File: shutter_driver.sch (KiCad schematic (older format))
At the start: 41 parts, among them J1 SHUTTER, J2 POWER, J3 I/O, J4 FRONT, Q1 2N3904, Q2 FQP30N06L-ND, Q3 2N3904, Q4 2N3904, Q5 Q_PMOS_GDS, SW1 SW_DPDT_x2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

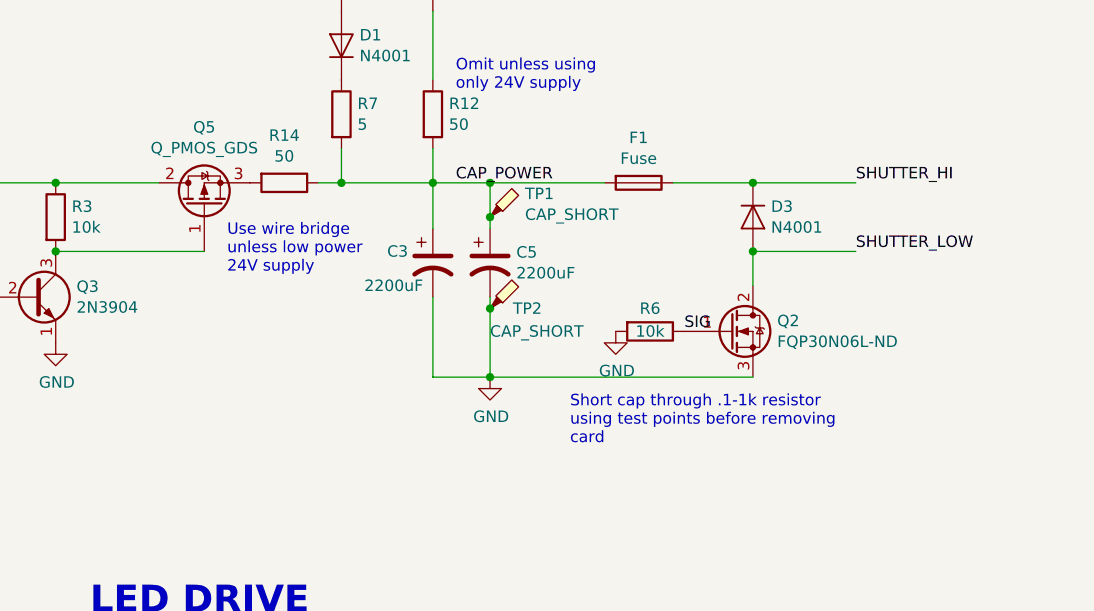
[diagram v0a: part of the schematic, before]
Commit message: fixed backward pmos
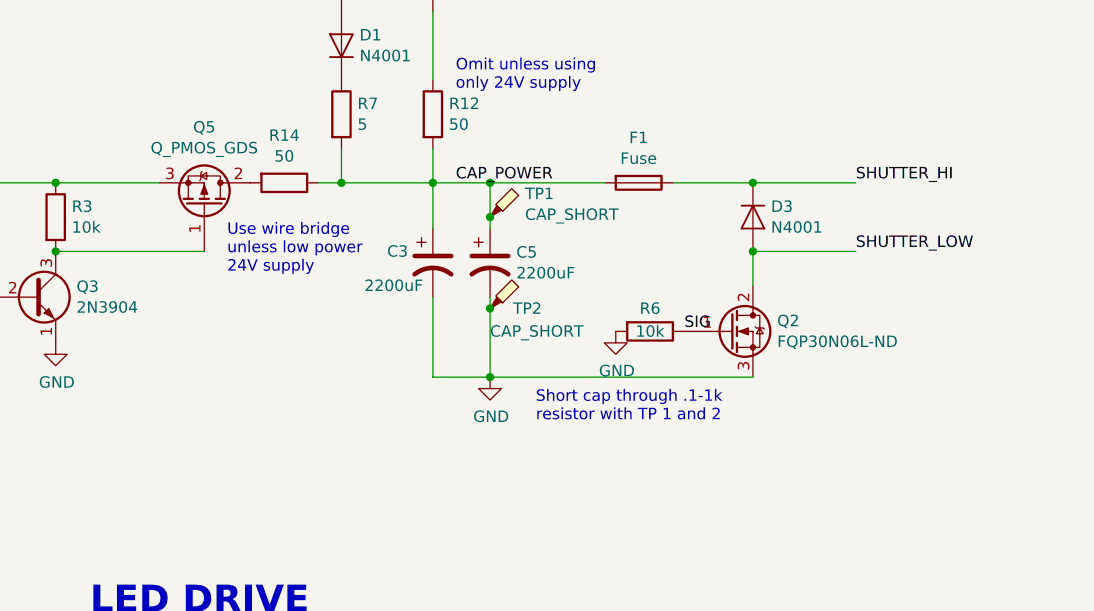
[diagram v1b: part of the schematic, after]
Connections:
- net +24V: now also Q5.3 (S); no longer Q5.2 (D)
- net at R14.2: now also Q5.2 (D); no longer Q5.3 (S)
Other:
- note added: "Short cap through .1-1k \nresistor with TP 1 and 2"
- note removed: "Short cap through .1-1k resistor\nusing test points before removing\ncard"
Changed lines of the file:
@@
 Sheet 1 1
 Title "NM LST400 Shutter Driver"
-Date ""
+Date "5.21.19"
 Rev "2.0"
 Comp "CSU Ultra Cold"
@@
 Wire Wire Line
 	4300 2500 4300 2800
-Text Notes 4650 3100 0    50   ~ 0
-Short cap through .1-1k resistor\nusing test points before removing\ncard
+Text Notes 4500 3000 0    50   ~ 0
+Short cap through .1-1k \nresistor with TP 1 and 2
 Wire Wire Line
 	4300 2800 5450 2800
@@
 F 3 "~" H 3050 2050 50  0001 C CNN
 	1    3050 2050
-	0    -1   -1   0
-$EndComp
-Wire Wire Line
+	0    1    -1   0
+$EndComp
+Wire Wire Line

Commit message: minor fixes including filter caps on rails of gates and comparator. note PMOS flipped in last commit.
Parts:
- added C2, C4, C7: .1u, symbol Device:C
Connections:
- net +5V: now also C2.2, C4.2, C7.2
- net GND: now also C2.1, C4.1, C7.1
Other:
- note added: "Pot sets interupt trigger point. \n2.5v is good starting point"
- note removed: "Pot sets interupt trigger point. \n2.5 v is good starting point"
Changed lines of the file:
@@
 Title "NM LST400 Shutter Driver"
 Date "5.21.19"
-Rev "2.0"
+Rev "2.1"
 Comp "CSU Ultra Cold"
 Comment1 ""
@@
 U 1 1 5C953346
 P 7600 4950
-F 0 "U6" H 7600 5275 50  0000 C CNN
-F 1 "SN74LVC1G86" H 7600 5184 50  0000 C CNN
+F 0 "U6" H 7550 4950 50  0000 C CNN
+F 1 "SN74LVC1G86" H 7300 5150 50  0000 C CNN
 F 2 "TO_SOT_Packages_SMD:SOT-23-5_HandSoldering" H 7600 4950 50  0001 C CNN
 F 3 "http://www.ti.com/lit/ds/symlink/sn74lvc1g86.pdf" H 7600 4950 50  0001 C CNN
@@
 U 1 1 5C97A9A3
 P 10250 2900
-F 0 "U9" V 10204 3088 50  0000 L CNN
-F 1 "SN74LVC1G86" V 10295 3088 50  0000 L CNN
+F 0 "U9" V 10200 2850 50  0000 L CNN
+F 1 "SN74LVC1G86" V 10050 3000 50  0000 L CNN
 F 2 "TO_SOT_Packages_SMD:SOT-23-5_HandSoldering" H 10250 2900 50  0001 C CNN
 F 3 "http://www.ti.com/lit/gpn/sn74HC86" H 10250 2900 50  0001 C CNN
@@
 SIG
 Text Notes 9050 5950 0    50   ~ 0
-Pot sets interupt trigger point. \n2.5 v is good starting point
+Pot sets interupt trigger point. \n2.5v is good starting point
 $Comp
 L Connector:TestPoint_Probe TP4
@@
 Text Label 2250 5150 1    50   ~ 0
 SHUTTER_RET
-Text Notes 9600 4450 0    50   ~ 0
+Text Notes 7450 5450 0    50   ~ 0
 RC network sets interupt time
 $Comp
@@
 Text Label 9900 1800 3    50   ~ 0
 LED_G-
-Text Notes 9850 1100 0    50   ~ 0
-RC network sets interupt time
 $Comp
 L Connector:Screw_Terminal_01x06 J4
@@
 L power:+5V #PWR0112
 U 1 1 5CB4EB9D
-P 7600 4850
-F 0 "#PWR0112" H 7600 4700 50  0001 C CNN
-F 1 "+5V" H 7615 5023 50  0000 C CNN
-F 2 "" H 7600 4850 50  0001 C CNN
-F 3 "" H 7600 4850 50  0001 C CNN
-	1    7600 4850
+P 7600 4650
+F 0 "#PWR0112" H 7600 4500 50  0001 C CNN
+F 1 "+5V" H 7500 4700 50  0000 C CNN
+F 2 "" H 7600 4650 50  0001 C CNN
+F 3 "" H 7600 4650 50  0001 C CNN
+	1    7600 4650
 	1    0    0    -1
 $EndComp
@@
 L power:+5V #PWR0113
 U 1 1 5CB4FC33
-P 10350 2900
-F 0 "#PWR0113" H 10350 2750 50  0001 C CNN
-F 1 "+5V" V 10365 3028 50  0000 L CNN
-F 2 "" H 10350 2900 50  0001 C CNN
-F 3 "" H 10350 2900 50  0001 C CNN
-	1    10350 2900
+P 10400 2900
+F 0 "#PWR0113" H 10400 2750 50  0001 C CNN
+F 1 "+5V" V 10415 3028 50  0000 L CNN
+F 2 "" H 10400 2900 50  0001 C CNN
+F 3 "" H 10400 2900 50  0001 C CNN
+	1    10400 2900
 	0    1    1    0
 $EndComp
@@
 Wire Wire Line
 	10250 3150 10250 3200
+$Comp
+L Device:C C2
+U 1 1 5CE5325D
+P 7750 4650
+F 0 "C2" V 7498 4650 50  0000 C CNN
+F 1 ".1u" V 7589 4650 50  0000 C CNN
+F 2 "" H 7788 4500 50  0001 C CNN
+F 3 "~" H 7750 4650 50  0001 C CNN
+	1    7750 4650
+	0    1    1    0
+$EndComp
+Connection ~ 7600 4650
+$Comp
+L power:GND #PWR0114
+U 1 1 5CE5337A
+P 7900 4650
+F 0 "#PWR0114" H 7900 4400 50  0001 C CNN
+F 1 "GND" V 7905 4522 50  0000 R CNN
+F 2 "" H 7900 4650 50  0001 C CNN
+F 3 "" H 7900 4650 50  0001 C CNN
+	1    7900 4650
+	0    -1   -1   0
+$EndComp
+$Comp
+L Device:C C7
+U 1 1 5CE535B0
+P 10400 3050
+F 0 "C7" V 10550 3050 50  0000 C CNN
+F 1 ".1u" V 10450 3150 50  0000 C CNN
+F 2 "" H 10438 2900 50  0001 C CNN
+F 3 "~" H 10400 3050 50  0001 C CNN
+	1    10400 3050
+	1    0    0    1
+$EndComp
+$Comp
+L power:GND #PWR0115
+U 1 1 5CE535B7
+P 10400 3200
+F 0 "#PWR0115" H 10400 2950 50  0001 C CNN
+F 1 "GND" V 10405 3072 50  0000 R CNN
+F 2 "" H 10400 3200 50  0001 C CNN
+F 3 "" H 10400 3200 50  0001 C CNN
+	1    10400 3200
+	-1   0    0    -1
+$EndComp
+Wire Wire Line
+	10350 2900 10400 2900
+Connection ~ 10400 2900
+$Comp
+L Device:C C4
+U 1 1 5CE5D1DA
+P 8700 4750
+F 0 "C4" V 8448 4750 50  0000 C CNN
+F 1 ".1u" V 8539 4750 50  0000 C CNN
+F 2 "" H 8738 4600 50  0001 C CNN
+F 3 "~" H 8700 4750 50  0001 C CNN
+	1    8700 4750
+	0    -1   1    0
+$EndComp
+$Comp
+L power:GND #PWR0116
+U 1 1 5CE5D1E1
+P 8550 4750
+F 0 "#PWR0116" H 8550 4500 50  0001 C CNN
+F 1 "GND" H 8555 4577 50  0000 C CNN
+F 2 "" H 8550 4750 50  0001 C CNN
+F 3 "" H 8550 4750 50  0001 C CNN
+	1    8550 4750
+	1    0    0    1
+$EndComp
+Connection ~ 8850 4750
+Wire Wire Line
+	7600 4650 7600 4850
 $EndSCHEMATC
